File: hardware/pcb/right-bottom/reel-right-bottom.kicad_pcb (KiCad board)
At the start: 2 copper layers, 143 x 86.6 mm, 5 parts

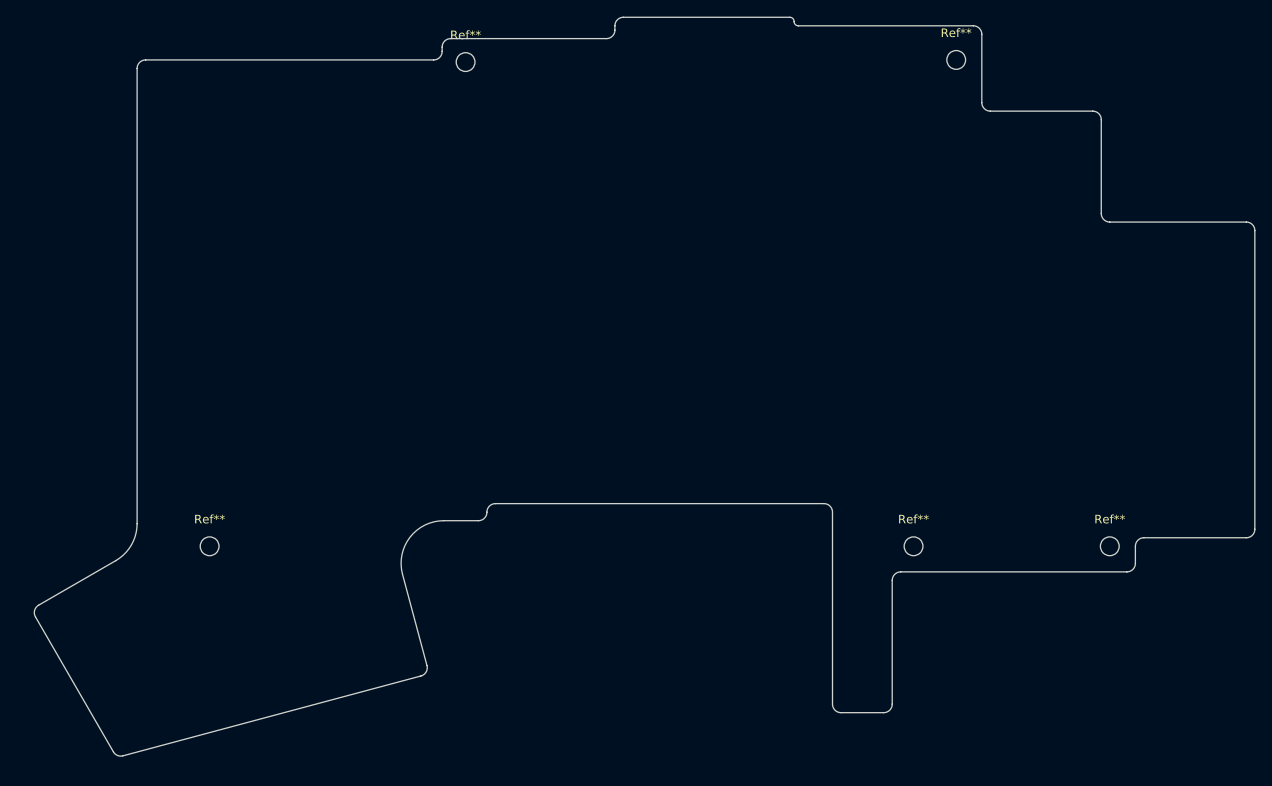
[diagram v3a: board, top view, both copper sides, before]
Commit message: Update right PCB and derived variants
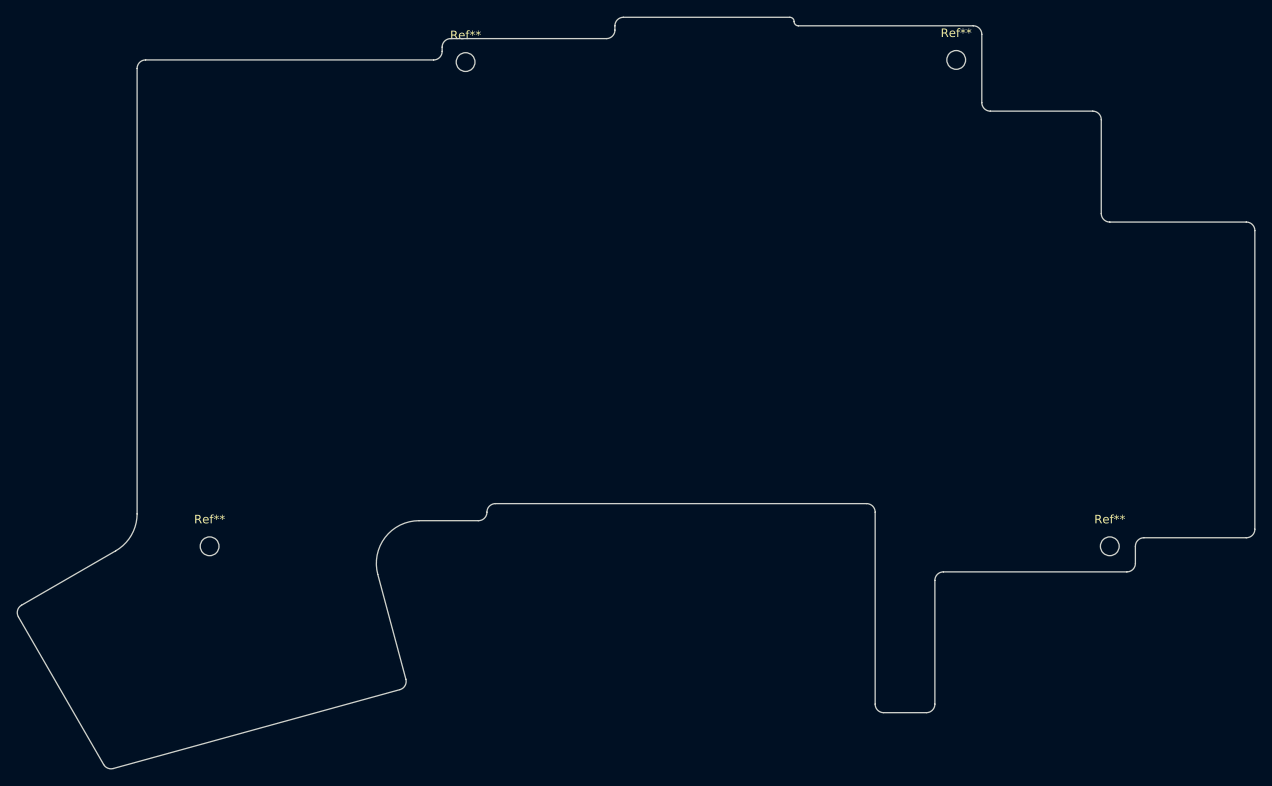
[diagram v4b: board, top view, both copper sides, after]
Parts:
- removed the Ref** at (140.5, 107.5)
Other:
- board size 143 x 86.6 mm -> 145 x 88.1 mm
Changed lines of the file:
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@@
 	(footprint "MountingHole:MountingHole_2.2mm_M2"
 		(layer "F.Cu")
-		(at 140.5 107.5)
+		(at 163.5 107.5)
 		(descr "Mounting Hole 2.2mm, M2, no annular, generated by kicad-footprint-generator mountinghole.py")
 		(tags "mountinghole M2")
@@
 	(footprint "MountingHole:MountingHole_2.2mm_M2"
 		(layer "F.Cu")
-		(at 163.5 107.5)
+		(at 145.5 50.5)
 		(descr "Mounting Hole 2.2mm, M2, no annular, generated by kicad-footprint-generator mountinghole.py")
 		(tags "mountinghole M2")
@@
 	(footprint "MountingHole:MountingHole_2.2mm_M2"
 		(layer "F.Cu")
-		(at 145.5 50.5)
+		(at 88 50.75)
 		(descr "Mounting Hole 2.2mm, M2, no annular, generated by kicad-footprint-generator mountinghole.py")
 		(tags "mountinghole M2")
@@
 	(footprint "MountingHole:MountingHole_2.2mm_M2"
 		(layer "F.Cu")
-		(at 88 50.75)
+		(at 58 107.5)
 		(descr "Mounting Hole 2.2mm, M2, no annular, generated by kicad-footprint-generator mountinghole.py")
 		(tags "mountinghole M2")
@@
 		(embedded_fonts no)
 	)
-	(footprint "MountingHole:MountingHole_2.2mm_M2"
-		(layer "F.Cu")
-		(at 58 107.5)
-		(descr "Mounting Hole 2.2mm, M2, no annular, generated by kicad-footprint-generator mountinghole.py")
-		(tags "mountinghole M2")
-		(property "Reference" "Ref**"
-			(at 0 -3.15 0)
-			(layer "F.SilkS")
-			(effects
-				(font
-					(size 1 1)
-					(thickness 0.15)
-				)
-			)
-		)
-		(property "Value" "MountingHole_2.2mm_M2"
-			(at 0 3.15 0)
-			(layer "F.Fab")
-			(effects
-				(font
-					(size 1 1)
-					(thickness 0.15)
-				)
-			)
-		)
-		(property "KiLib_Generator" "mounting_hardware/mounting_hole"
-			(at 0 0 0)
-			(layer "F.SilkS")
-			(hide yes)
-			(effects
-				(font
-					(size 1 1)
-					(thickness 0.15)
-				)
-			)
-		)
-		(attr exclude_from_pos_files exclude_from_bom)
-		(duplicate_pad_numbers_are_jumpers no)
-		(fp_circle
-			(center 0 0)
-			(end 2.2 0)
-			(stroke
-				(width 0.15)
-				(type solid)
-			)
-			(fill no)
-			(layer "Cmts.User")
-		)
-		(fp_circle
-			(center 0 0)
-			(end 2.45 0)
-			(stroke
-				(width 0.05)
-				(type solid)
-			)
-			(fill no)
-			(layer "F.CrtYd")
-		)
-		(fp_text user "${REFERENCE}"
-			(at 0 0 0)
-			(layer "F.Fab")
-			(effects
-				(font
-					(size 1 1)
-					(thickness 0.15)
-				)
-			)
-		)
-		(pad "" np_thru_hole circle
-			(at 0 0)
-			(size 2.2 2.2)
-			(drill 2.2)
-			(layers "*.Cu" "*.Mask")
-		)
-		(embedded_fonts no)
-	)
-	(gr_arc
-		(start 37.589746 115.772758)
-		(mid 37.489877 115.013958)
-		(end 37.955771 114.406733)
-		(stroke
-			(width 0.05)
-			(type default)
-		)
-		(layer "Edge.Cuts")
-	)
-	(gr_line
-		(start 37.589746 115.772758)
-		(end 46.722209 131.590648)
+	(gr_arc
+		(start 35.589762 115.772786)
+		(mid 35.489859 115.013966)
+		(end 35.955785 114.406758)
+		(stroke
+			(width 0.05)
+			(type default)
+		)
+		(layer "Edge.Cuts")
+	)
+	(gr_line
+		(start 35.589762 115.772786)
+		(end 45.582283 133.0802)
 		(stroke
 			(width 0.05)
@@
 		(layer "Edge.Cuts")
 	)
-	(gr_line
-		(start 37.955771 114.406733)
-		(end 47 109.185045)
+	(gr_arc
+		(start 46.713675 133.544345)
+		(mid 46.068759 133.505375)
+		(end 45.582283 133.0802)
+		(stroke
+			(width 0.05)
+			(type default)
+		)
+		(layer "Edge.Cuts")
+	)
+	(gr_line
+		(start 46.713675 133.544345)
+		(end 80.29895 124.300482)
 		(stroke
 			(width 0.05)
@@
 		(layer "Edge.Cuts")
 	)
-	(gr_arc
-		(start 47.847054 132.056574)
-		(mid 47.205532 132.014546)
-		(end 46.722209 131.590648)
-		(stroke
-			(width 0.05)
-			(type default)
+	(gr_line
+		(start 47 108.030377)
+		(end 35.955785 114.406758)
+		(stroke
+			(width 0.05)
+			(type solid)
 		)
 		(layer "Edge.Cuts")
@@
 	(gr_line
 		(start 49.5 51.5)
-		(end 49.5 104.854918)
+		(end 49.5 103.70025)
 		(stroke
 			(width 0.05)
@@
 	)
 	(gr_arc
-		(start 49.5 104.854918)
-		(mid 48.83012 107.354912)
-		(end 47 109.185045)
+		(start 49.5 103.70025)
+		(mid 48.830108 106.200232)
+		(end 47 108.030377)
 		(stroke
 			(width 0.05)
@@
 	)
 	(gr_arc
-		(start 80.609457 110.794095)
-		(mid 81.47232 106.456193)
-		(end 85.439086 104.5)
-		(stroke
-			(width 0.05)
-			(type default)
-		)
-		(layer "Edge.Cuts")
-	)
-	(gr_line
-		(start 82.764485 122.700476)
-		(end 47.847054 132.056574)
+		(start 77.708196 110.794087)
+		(mid 78.571063 106.45619)
+		(end 82.537827 104.5)
+		(stroke
+			(width 0.05)
+			(type default)
+		)
+		(layer "Edge.Cuts")
+	)
+	(gr_line
+		(start 80.999508 123.077517)
+		(end 77.708196 110.794087)
 		(stroke
 			(width 0.05)
@@
 		(layer "Edge.Cuts")
 	)
-	(gr_line
-		(start 83.471592 121.475731)
-		(end 80.609457 110.794095)
-		(stroke
-			(width 0.05)
-			(type solid)
-		)
-		(layer "Edge.Cuts")
-	)
-	(gr_arc
-		(start 83.471592 121.475731)
-		(mid 83.371665 122.234514)
-		(end 82.764485 122.700476)
+	(gr_arc
+		(start 80.999508 123.077517)
+		(mid 80.901298 123.833393)
+		(end 80.29895 124.300482)
+		(stroke
+			(width 0.05)
+			(type default)
+		)
+		(layer "Edge.Cuts")
+	)
+	(gr_line
+		(start 82.537827 104.5)
+		(end 89.5 104.5)
 		(stroke
 			(width 0.05)
@@
 		(layer "Edge.Cuts")
 	)
-	(gr_line
-		(start 89.5 104.5)
-		(end 85.439086 104.5)
-		(stroke
-			(width 0.05)
-			(type default)
-		)
-		(layer "Edge.Cuts")
-	)
 	(gr_arc
 		(start 90.5 103.5)
@@
 	(gr_line
 		(start 91.5 102.5)
-		(end 130 102.5)
+		(end 135 102.5)
 		(stroke
 			(width 0.05)
@@
 	)
 	(gr_arc
-		(start 130 102.5)
-		(mid 130.707107 102.792893)
-		(end 131 103.5)
-		(stroke
-			(width 0.05)
-			(type default)
-		)
-		(layer "Edge.Cuts")
-	)
-	(gr_line
-		(start 131 126)
-		(end 131 103.5)
+		(start 135 102.5)
+		(mid 135.707107 102.792893)
+		(end 136 103.5)
+		(stroke
+			(width 0.05)
+			(type default)
+		)
+		(layer "Edge.Cuts")
+	)
+	(gr_line
+		(start 136 126)
+		(end 136 103.5)
 		(stroke
 			(width 0.05)
@@
 	)
 	(gr_arc
-		(start 132 127)
-		(mid 131.292893 126.707107)
-		(end 131 126)
-		(stroke
-			(width 0.05)
-			(type default)
-		)
-		(layer "Edge.Cuts")
-	)
-	(gr_line
 		(start 137 127)
-		(end 132 127)
+		(mid 136.292893 126.707107)
+		(end 136 126)
+		(stroke
+			(width 0.05)
+			(type default)
+		)
+		(layer "Edge.Cuts")
+	)
+	(gr_line
+		(start 142 127)
+		(end 137 127)
 		(stroke
 			(width 0.05)
@@
 	)
 	(gr_line
-		(start 138 111.5)
-		(end 138 126)
+		(start 143 111.5)
+		(end 143 126)
 		(stroke
 			(width 0.05)
@@
 	)
 	(gr_arc
-		(start 138 111.5)
-		(mid 138.292893 110.792893)
-		(end 139 110.5)
-		(stroke
-			(width 0.05)
-			(type default)
-		)
-		(layer "Edge.Cuts")
-	)
-	(gr_arc
-		(start 138 126)
-		(mid 137.707107 126.707107)
-		(end 137 127)
+		(start 143 111.5)
+		(mid 143.292893 110.792893)
+		(end 144 110.5)
+		(stroke
+			(width 0.05)
+			(type default)
+		)
+		(layer "Edge.Cuts")
+	)
+	(gr_arc
+		(start 143 126)
+		(mid 142.707107 126.707107)
+		(end 142 127)
 		(stroke
 			(width 0.05)
@@
 	(gr_line
 		(start 165.5 110.5)
-		(end 139 110.5)
-		(stroke
-			(width 0.05)
+		(end 144 110.5)
+		(stroke
+			(width 0.05)
